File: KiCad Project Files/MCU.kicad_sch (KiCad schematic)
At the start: 24 parts, among them SW1 Reset, U1 RP2040, U2 W25Q128JVS, Y1 12MHz

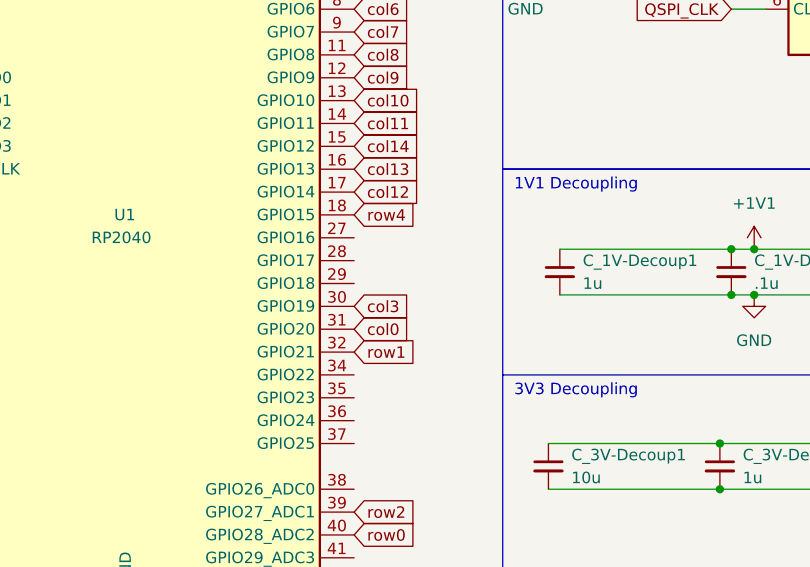
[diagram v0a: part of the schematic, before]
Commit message: Add leds to pcb
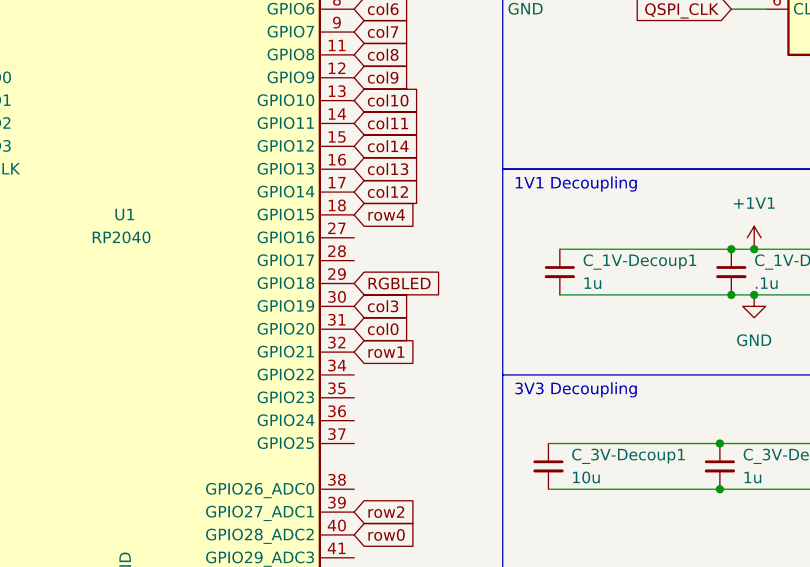
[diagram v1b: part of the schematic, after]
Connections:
- net RGBLED: now reaches U1.29 (GPIO18)
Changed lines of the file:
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@@
+    )
+  )
+  (global_label "RGBLED" (shape input) (at 88.9 88.9 0) (fields_autoplaced)
+    (effects (font (size 1.27 1.27)) (justify left))
+    (property "Intersheetrefs" "${INTERSHEET_REFS}" (at 99.0629 88.9 0)
+      (effects (font (size 1.27 1.27)) (justify left) hide)
     )
   )
